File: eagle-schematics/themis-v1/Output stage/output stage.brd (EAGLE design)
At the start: 66.6 x 47.9 mm, 18 parts, among them IC1 NE5534AN

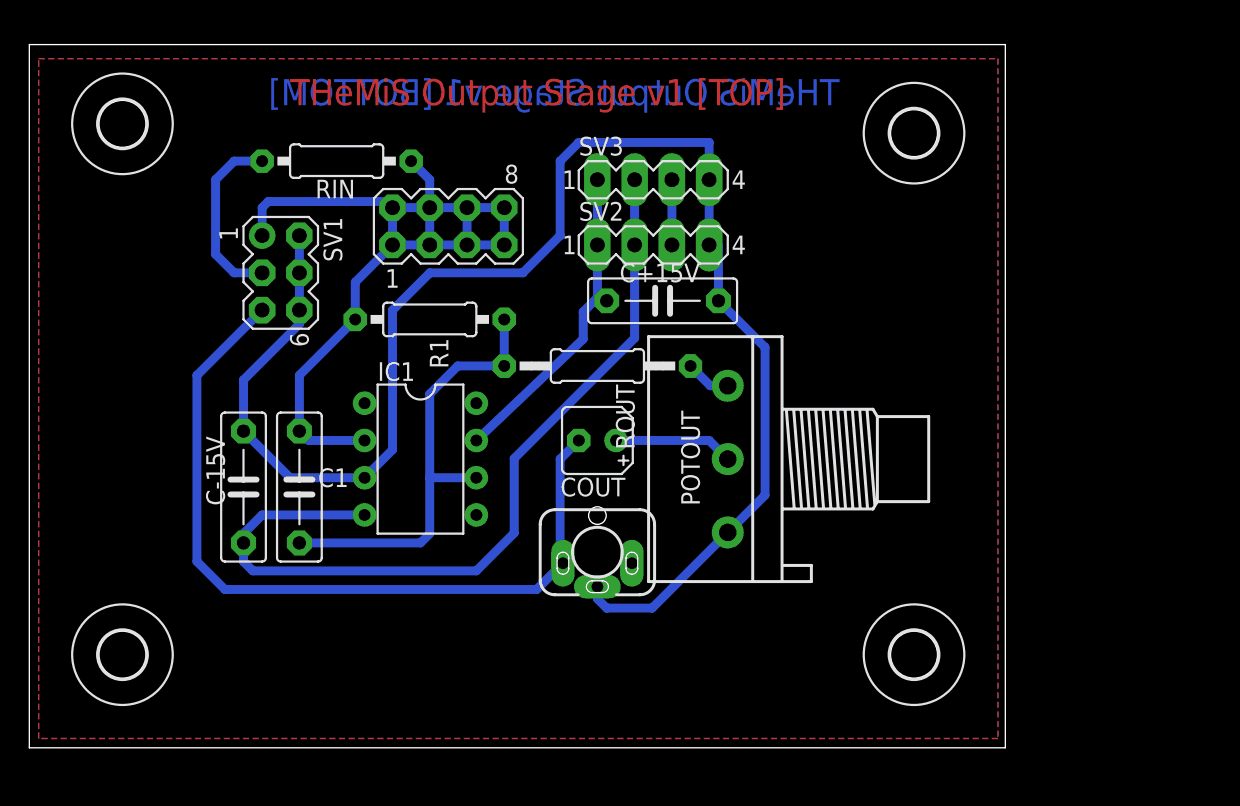
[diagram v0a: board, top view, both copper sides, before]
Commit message: Improved schematics, added analog chips library
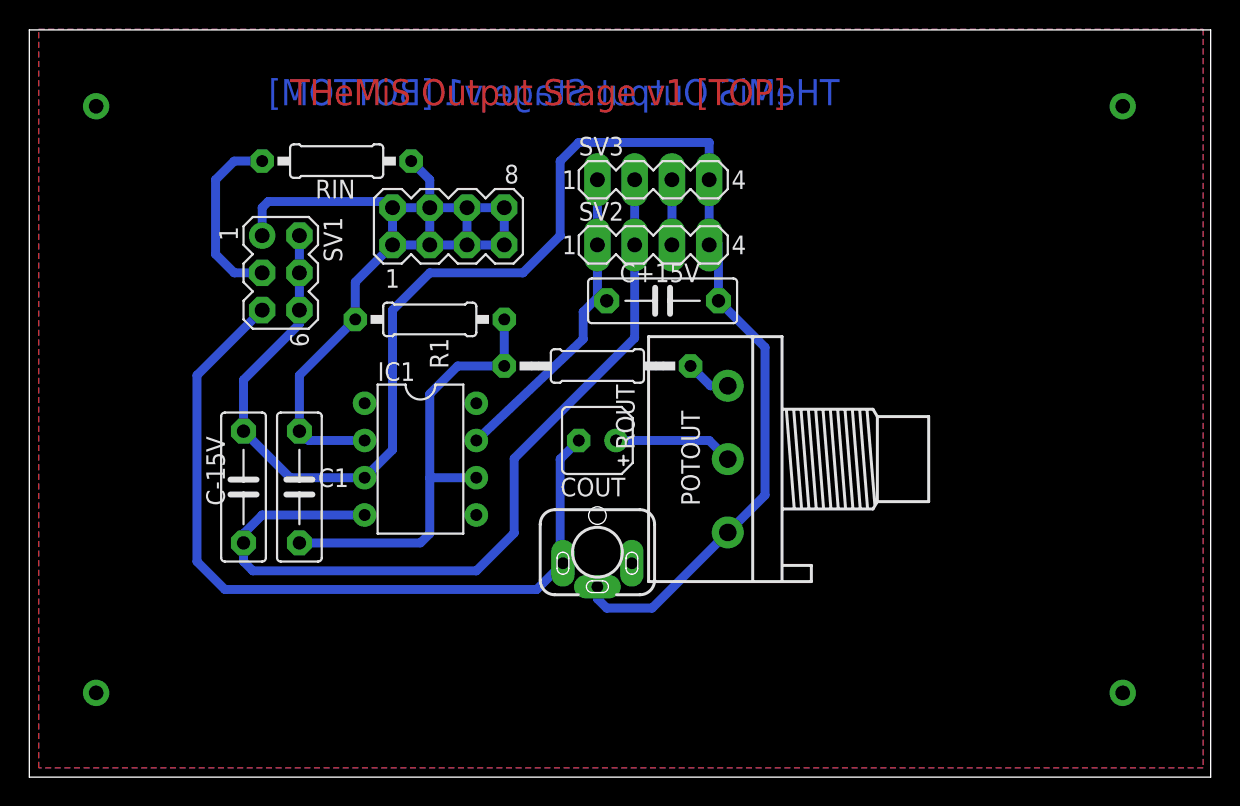
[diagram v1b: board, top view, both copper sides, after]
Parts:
- removed U$1, U$2, U$3, U$4: (no value), holes:3,2
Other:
- board size 66.6 x 47.9 mm -> 80.6 x 50.9 mm
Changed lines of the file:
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@@
 <?xml version="1.0" encoding="utf-8"?>
 <!DOCTYPE eagle SYSTEM "eagle.dtd">
-<eagle version="9.3.1">
+<eagle version="9.5.0">
 <drawing>
 <settings>
@@
 <setting verticaltext="up"/>
 </settings>
-<grid distance="25" unitdist="mil" unit="mil" style="lines" multiple="1" display="no" altdistance="5" altunitdist="mil" altunit="mil"/>
+<grid distance="1" unitdist="mm" unit="mm" style="lines" multiple="1" display="yes" altdistance="5" altunitdist="mil" altunit="mil"/>
 <layers>
-<layer number="1" name="Top" color="4" fill="1" visible="no" active="yes"/>
+<layer number="1" name="Top" color="4" fill="1" visible="yes" active="yes"/>
 <layer number="2" name="Route2" color="16" fill="1" visible="no" active="no"/>
 <layer number="3" name="Route3" color="17" fill="1" visible="no" active="no"/>
@@
 <layer number="17" name="Pads" color="2" fill="1" visible="yes" active="yes"/>
 <layer number="18" name="Vias" color="2" fill="1" visible="yes" active="yes"/>
-<layer number="19" name="Unrouted" color="6" fill="1" visible="no" active="yes"/>
-<layer number="20" name="Dimension" color="24" fill="1" visible="no" active="yes"/>
-<layer number="21" name="tPlace" color="7" fill="1" visible="no" active="yes"/>
-<layer number="22" name="bPlace" color="7" fill="1" visible="no" active="yes"/>
-<layer number="23" name="tOrigins" color="15" fill="1" visible="no" active="yes"/>
-<layer number="24" name="bOrigins" color="15" fill="1" visible="no" active="yes"/>
-<layer number="25" name="tNames" color="7" fill="1" visible="no" active="yes"/>
-<layer number="26" name="bNames" color="7" fill="1" visible="no" active="yes"/>
+<layer number="19" name="Unrouted" color="6" fill="1" visible="yes" active="yes"/>
+<layer number="20" name="Dimension" color="24" fill="1" visible="yes" active="yes"/>
+<layer number="21" name="tPlace" color="7" fill="1" visible="yes" active="yes"/>
+<layer number="22" name="bPlace" color="7" fill="1" visible="yes" active="yes"/>
+<layer number="23" name="tOrigins" color="15" fill="1" visible="yes" active="yes"/>
+<layer number="24" name="bOrigins" color="15" fill="1" visible="yes" active="yes"/>
+<layer number="25" name="tNames" color="7" fill="1" visible="yes" active="yes"/>
+<layer number="26" name="bNames" color="7" fill="1" visible="yes" active="yes"/>
 <layer number="27" name="tValues" color="7" fill="1" visible="no" active="yes"/>
 <layer number="28" name="bValues" color="7" fill="1" visible="no" active="yes"/>
@@
 <layer number="37" name="tTest" color="7" fill="1" visible="no" active="yes"/>
 <layer number="38" name="bTest" color="7" fill="1" visible="no" active="yes"/>
-<layer number="39" name="tKeepout" color="4" fill="11" visible="no" active="yes"/>
-<layer number="40" name="bKeepout" color="1" fill="11" visible="no" active="yes"/>
-<layer number="41" name="tRestrict" color="4" fill="10" visible="no" active="yes"/>
-<layer number="42" name="bRestrict" color="1" fill="10" visible="no" active="yes"/>
+<layer number="39" name="tKeepout" color="4" fill="11" visible="yes" active="yes"/>
+<layer number="40" name="bKeepout" color="1" fill="11" visible="yes" active="yes"/>
+<layer number="41" name="tRestrict" color="4" fill="10" visible="yes" active="yes"/>
+<layer number="42" name="bRestrict" color="1" fill="10" visible="yes" active="yes"/>
 <layer number="43" name="vRestrict" color="2" fill="10" visible="no" active="yes"/>
 <layer number="44" name="Drills" color="7" fill="1" visible="no" active="yes"/>
 <layer number="45" name="Holes" color="7" fill="1" visible="no" active="yes"/>
 <layer number="46" name="Milling" color="3" fill="1" visible="no" active="yes"/>
-<layer number="47" name="Measures" color="7" fill="1" visible="no" active="yes"/>
+<layer number="47" name="Measures" color="7" fill="1" visible="yes" active="yes"/>
 <layer number="48" name="Document" color="7" fill="1" visible="no" active="yes"/>
 <layer number="49" name="Reference" color="7" fill="1" visible="no" active="yes"/>
 <layer number="50" name="dxf" color="7" fill="1" visible="no" active="no"/>
-<layer number="51" name="tDocu" color="7" fill="1" visible="no" active="yes"/>
-<layer number="52" name="bDocu" color="7" fill="1" visible="no" active="yes"/>
+<layer number="51" name="tDocu" color="7" fill="1" visible="yes" active="yes"/>
+<layer number="52" name="bDocu" color="7" fill="1" visible="yes" active="yes"/>
 <layer number="53" name="tGND_GNDA" color="7" fill="9" visible="no" active="no"/>
 <layer number="54" name="bGND_GNDA" color="1" fill="9" visible="no" active="no"/>
@@
 <board>
 <plain>
-<wire x1="4.445" y1="8.255" x2="70.995" y2="8.255" width="0" layer="20"/>
-<wire x1="70.995" y1="8.255" x2="70.995" y2="56.205" width="0" layer="20"/>
-<wire x1="70.995" y1="56.205" x2="4.445" y2="56.205" width="0" layer="20"/>
-<wire x1="4.445" y1="56.205" x2="4.445" y2="8.255" width="0" layer="20"/>
+<wire x1="4.445" y1="6.255" x2="84.995" y2="6.255" width="0" layer="20"/>
+<wire x1="84.995" y1="6.255" x2="84.995" y2="57.205" width="0" layer="20"/>
+<wire x1="84.995" y1="57.205" x2="4.445" y2="57.205" width="0" layer="20"/>
+<wire x1="4.445" y1="57.205" x2="4.445" y2="6.255" width="0" layer="20"/>
 <text x="59.69" y="52.07" size="1.778" layer="16" rot="MR0">THeMiS Output Stage v1 [BOTTOM]</text>
 <text x="22.225" y="52.07" size="1.778" layer="1">THeMiS Output Stage v1 [TOP]</text>
+<dimension x1="9" y1="52" x2="9" y2="12" x3="-8" y3="32" textsize="1.778" layer="47"/>
+<dimension x1="9" y1="52" x2="9" y2="57" x3="-8" y3="54.5" textsize="1.778" layer="47"/>
+<dimension x1="9" y1="12" x2="9" y2="7" x3="-8" y3="9.5" textsize="1.778" layer="47"/>
+<dimension x1="9" y1="52" x2="79" y2="52" x3="44" y3="59" textsize="1.778" layer="47"/>
+<dimension x1="9" y1="52" x2="4" y2="52" x3="6.5" y3="59" textsize="1.778" layer="47"/>
+<dimension x1="79" y1="52" x2="84" y2="52" x3="81.5" y3="59" textsize="1.778" layer="47"/>
+<wire x1="9" y1="12" x2="79" y2="12" width="0.1524" layer="47"/>
+<wire x1="79" y1="12" x2="79" y2="52" width="0.1524" layer="47"/>
+<wire x1="79" y1="52" x2="9" y2="52" width="0.1524" layer="47"/>
+<wire x1="9" y1="52" x2="9" y2="12" width="0.1524" layer="47"/>
 </plain>
 <attributes>
@@
 <attribute name="VALUE" x="47.625" y="48.641" size="1.27" layer="27" ratio="10"/>
 </element>
-<element name="U$1" library="holes" library_urn="urn:adsk.eagle:library:237" package="3,2" package3d_urn="urn:adsk.eagle:package:14275/1" value="" x="64.77" y="50.165" smashed="yes"/>
-<element name="U$2" library="holes" library_urn="urn:adsk.eagle:library:237" package="3,2" package3d_urn="urn:adsk.eagle:package:14275/1" value="" x="10.795" y="14.605" smashed="yes"/>
-<element name="U$3" library="holes" library_urn="urn:adsk.eagle:library:237" package="3,2" package3d_urn="urn:adsk.eagle:package:14275/1" value="" x="64.77" y="14.605" smashed="yes"/>
-<element name="U$4" library="holes" library_urn="urn:adsk.eagle:library:237" package="3,2" package3d_urn="urn:adsk.eagle:package:14275/1" value="" x="10.795" y="50.8" smashed="yes"/>
 </elements>
 <signals>
@@
 <contactref element="SV3" pad="4"/>
 <polygon width="0.6096" layer="1" isolate="0.6096">
-<vertex x="5.08" y="55.245"/>
-<vertex x="70.485" y="55.245"/>
-<vertex x="70.485" y="8.89"/>
-<vertex x="6.35" y="8.89"/>
-<vertex x="5.08" y="8.89"/>
+<vertex x="5.08" y="57.245"/>
+<vertex x="84.485" y="57.245"/>
+<vertex x="84.485" y="6.89"/>
+<vertex x="5.08" y="6.89"/>
 </polygon>
 <polygon width="0.6096" layer="16" isolate="0.6096">
-<vertex x="5.08" y="55.245"/>
-<vertex x="70.485" y="55.245"/>
-<vertex x="70.485" y="8.89"/>
-<vertex x="5.08" y="8.89"/>
+<vertex x="5.08" y="57.245"/>
+<vertex x="84.485" y="57.245"/>
+<vertex x="84.485" y="6.89"/>
+<vertex x="5.08" y="6.89"/>
 </polygon>
 <contactref element="IC1" pad="3"/>
@@
 <wire x1="48.26" y1="46.99" x2="48.26" y2="42.545" width="0.6096" layer="16"/>
 </signal>
+<signal name="N$1">
+<via x="9" y="52" extent="1-16" drill="1" shape="square"/>
+</signal>
+<signal name="N$2">
+<via x="9" y="12" extent="1-16" drill="1" shape="square"/>
+</signal>
+<signal name="N$3">
+<via x="79" y="12" extent="1-16" drill="1" shape="square"/>
+</signal>
+<signal name="N$4">
+<via x="79" y="52" extent="1-16" drill="1" shape="square"/>
+</signal>
 </signals>
 <mfgpreviewcolors>
@@
 <mfgpreviewcolor name="substratecolor" color="0xFF786E46"/>
 </mfgpreviewcolors>
-<errors>
-</errors>
 </board>
 </drawing>
